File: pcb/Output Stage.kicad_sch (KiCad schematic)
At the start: 18 parts

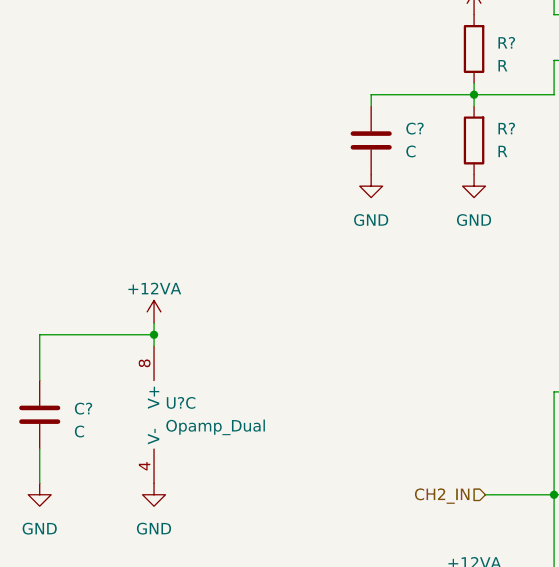
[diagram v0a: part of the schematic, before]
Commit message: Completed schematic oranization and components connection
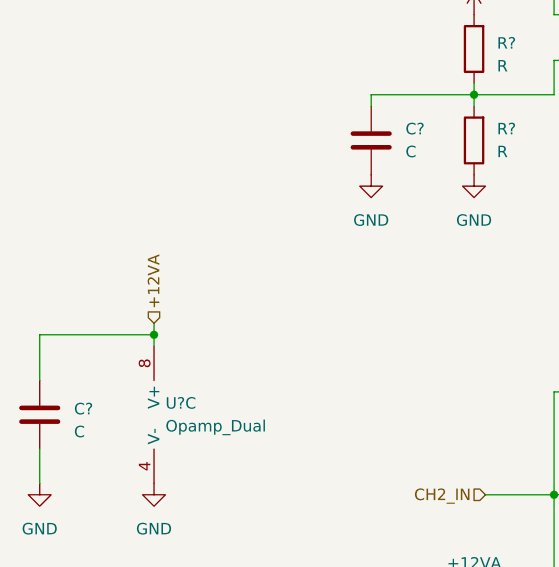
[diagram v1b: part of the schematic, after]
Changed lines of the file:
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@@
+    (effects (font (size 1.27 1.27)) (justify left))
+  )
+  (hierarchical_label "+12VA" (shape input) (at 54.61 97.79 90) (fields_autoplaced)
     (effects (font (size 1.27 1.27)) (justify left))
   )
@@
         )
       )
-    )
-  )
-  (symbol (lib_id "power:+12VA") (at 54.61 97.79 0) (unit 1)
-    (in_bom yes) (on_board yes) (dnp no) (fields_autoplaced)
-    (property "Reference" "#PWR02" (at 54.61 101.6 0)
-      (effects (font (size 1.27 1.27)) hide)
-    )
-    (property "Value" "+12VA" (at 54.61 93.98 0)
-      (effects (font (size 1.27 1.27)))
-    )
-    (property "Footprint" "" (at 54.61 97.79 0)
-      (effects (font (size 1.27 1.27)) hide)
-    )
-    (property "Datasheet" "" (at 54.61 97.79 0)
-      (effects (font (size 1.27 1.27)) hide)
-    )
-    (pin "1")
-    (instances
-      (project "Signal Generator"
-        (path "/f6255c48-6253-4c69-a6db-1ceaf4eff04d"
-          (reference "#PWR02") (unit 1)
-        )
-        (path "/f6255c48-6253-4c69-a6db-1ceaf4eff04d/d7478301-eb73-4c22-aaa0-fe451be16808"
-          (reference "#PWR0117") (unit 1)
-        )
-      )

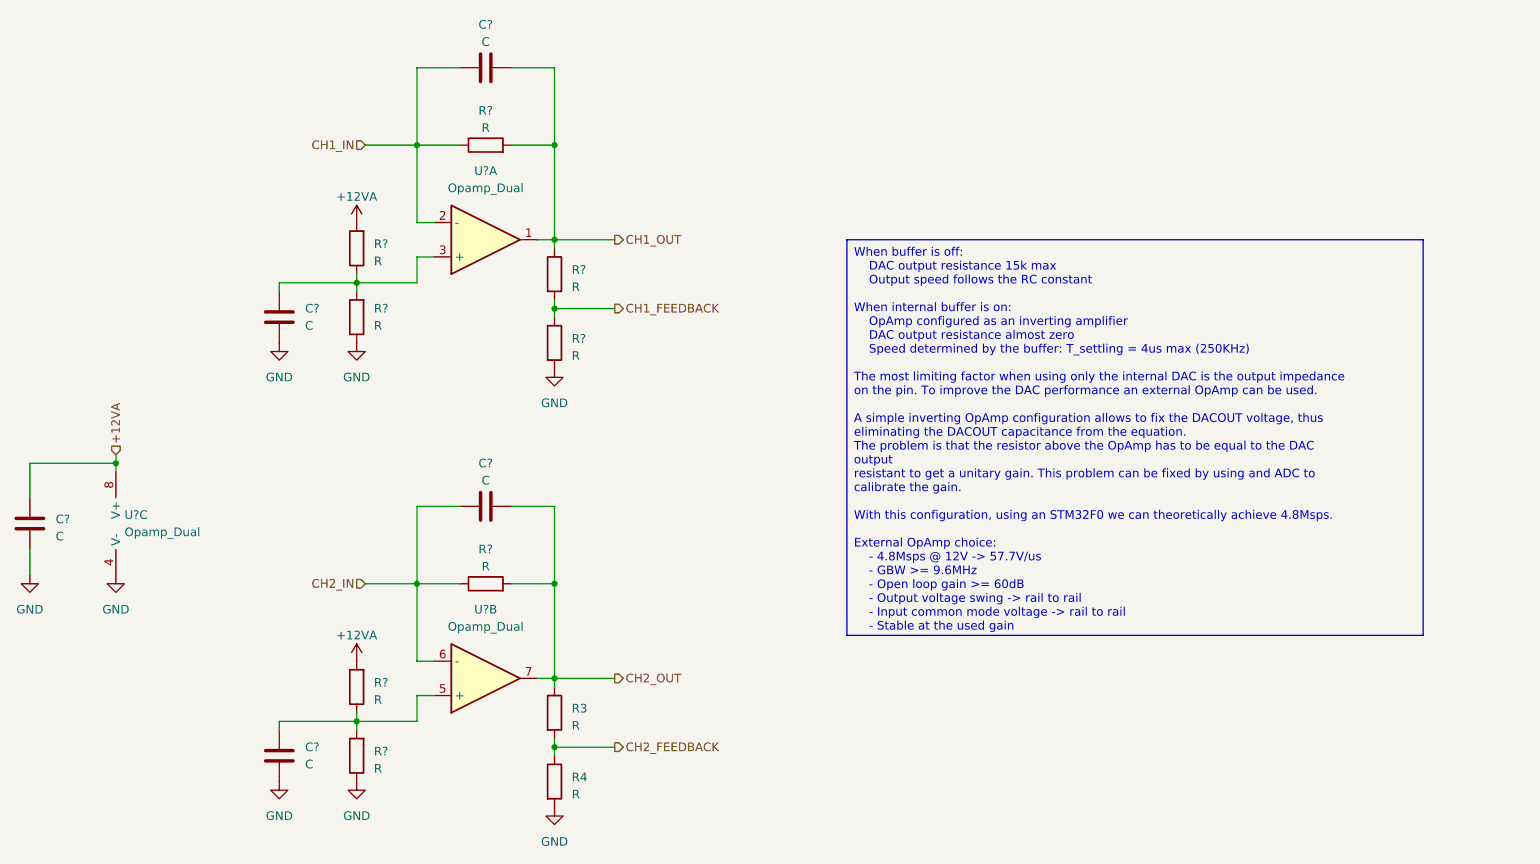
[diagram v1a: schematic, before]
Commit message: Added micro SD and RGB led to schematic. Also added components part numbers
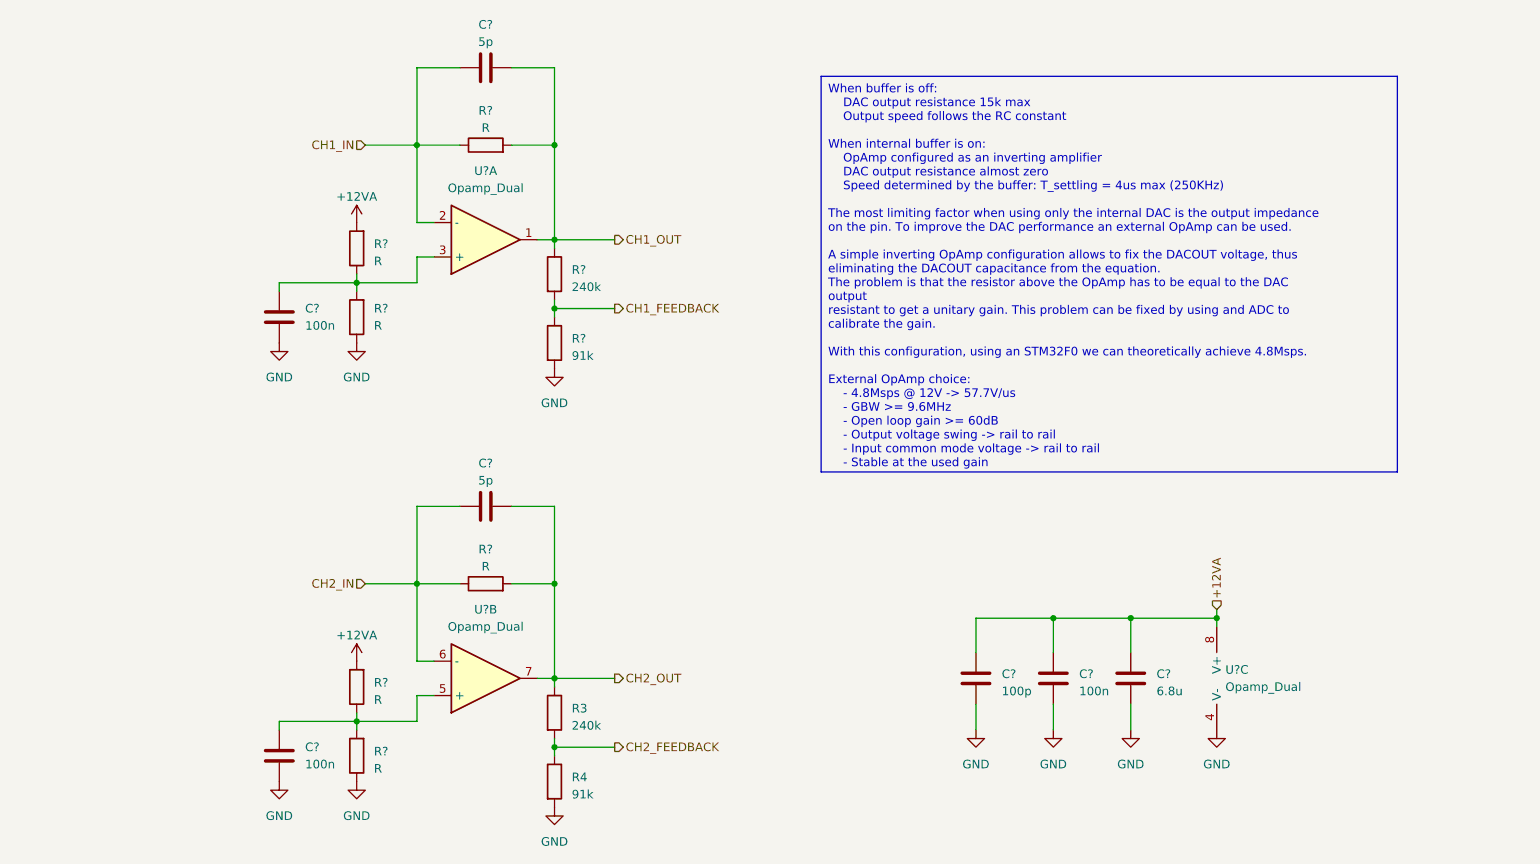
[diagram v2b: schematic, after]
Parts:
- added C?: 100n, Capacitor_SMD:C_0603_1608Metric, symbol Device:C
- added C?: 100p, Capacitor_SMD:C_0603_1608Metric, symbol Device:C
- C? (x2): value C -> 5p; PN (none) -> GQM1875C2E5R0CB12D
- C?: value C -> 6.8u; PN (none) -> GRM1885C1H6R8CA1D
- C? (x2): value C -> 100n; PN (none) -> GCM188R71H104KA57J
- R3, R?: value R -> 240k; PN (none) -> ERJ-3RED2403V
- R4, R?: value R -> 91k; PN (none) -> ERJ-PB3B9102V
- U? (x3): PN (none) -> SN10502D
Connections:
- net +12VA: now also C?.1, C?.1
- net GND: now also C?.2, C?.2
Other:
- moved on the sheet: C?, U?C

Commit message: Completed schematic and tried some simulations
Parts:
- removed C? (x2): 5p, Capacitor_SMD:C_0603_1608Metric, symbol Device:C
- added C? (x2): 0.5p, Capacitor_SMD:C_0603_1608Metric, symbol Device:C
- C?: PN GRM1885C1H6R8CA1D -> GRM1885C1H6R8CA01D
- R? (x2): value R -> 1.33k; PN (none) -> ERJ-PB3B1331V
- R? (x2): value R -> 4.75k; PN (none) -> ERJ-PB3B4751V
- R? (x2): value R -> 46.4k; PN (none) -> ERJ-PB3B4642V
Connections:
- net CH1_IN: now also C?.1
- net CH1_OUT: now also C?.2
- net CH2_IN: now also C?.1
- net CH2_OUT: now also C?.2

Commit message: Completed PCB and prepared production files
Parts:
- U? (x3): PN SN10502D -> OPA2810IDR
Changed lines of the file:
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@@
       (effects (font (size 1.27 1.27)) hide)
     )
-    (property "PN" "SN10502D" (at 109.22 66.04 0)
+    (property "PN" "OPA2810IDR" (at 109.22 66.04 0)
       (effects (font (size 1.27 1.27)) hide)
     )
@@
       (effects (font (size 1.27 1.27)) hide)
     )
-    (property "PN" "SN10502D" (at 109.22 130.81 0)
+    (property "PN" "OPA2810IDR" (at 109.22 130.81 0)
       (effects (font (size 1.27 1.27)) hide)
     )
@@
       (effects (font (size 1.27 1.27)) hide)
     )
-    (property "PN" "SN10502D" (at 219.71 130.81 0)
-      (effects (font (size 1.27 1.27)) hide)
-    )
+    (property "PN" "OPA2810IDR" (at 219.71 130.81 0)
+      (effects (font (size 1.27 1.27)) hide)
+    )

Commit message: Fixed FTDI connection to the stm32
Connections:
- net CH1_FEEDBACK: now also R3.2, R4.1; no longer R?.1, R?.2
- net CH1_IN: now also C?.1, R?.1, U?.6 (-); no longer C?.1, R?.1, U?.2 (-)
- net CH1_OUT: now also C?.2, R3.1, R?.2, U?.7; no longer C?.2, R?.1, R?.2, U?.1
- net CH2_FEEDBACK: now also R?.1, R?.2; no longer R3.2, R4.1
- net CH2_IN: now also C?.1, R?.1, U?.2 (-); no longer C?.1, R?.1, U?.6 (-)
- net CH2_OUT: now also C?.2, R?.1, R?.2, U?.1; no longer C?.2, R3.1, R?.2, U?.7
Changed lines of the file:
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@@
     (effects (font (size 1.27 1.27)) (justify left top))
   )
-  (hierarchical_label "CH1_OUT" (shape output) (at 128.27 66.04 0) (fields_autoplaced)
+  (hierarchical_label "CH2_OUT" (shape output) (at 128.27 66.04 0) (fields_autoplaced)
     (effects (font (size 1.27 1.27)) (justify left))
   )
@@
     (effects (font (size 1.27 1.27)) (justify left))
   )
-  (hierarchical_label "CH2_IN" (shape input) (at 91.44 116.84 180) (fields_autoplaced)
+  (hierarchical_label "CH1_IN" (shape input) (at 91.44 116.84 180) (fields_autoplaced)
     (effects (font (size 1.27 1.27)) (justify right))
   )
-  (hierarchical_label "CH2_OUT" (shape output) (at 128.27 130.81 0) (fields_autoplaced)
+  (hierarchical_label "CH1_OUT" (shape output) (at 128.27 130.81 0) (fields_autoplaced)
     (effects (font (size 1.27 1.27)) (justify left))
   )
-  (hierarchical_label "CH2_FEEDBACK" (shape output) (at 128.27 140.97 0) (fields_autoplaced)
+  (hierarchical_label "CH1_FEEDBACK" (shape output) (at 128.27 140.97 0) (fields_autoplaced)
     (effects (font (size 1.27 1.27)) (justify left))
   )
-  (hierarchical_label "CH1_FEEDBACK" (shape output) (at 128.27 76.2 0) (fields_autoplaced)
+  (hierarchical_label "CH2_FEEDBACK" (shape output) (at 128.27 76.2 0) (fields_autoplaced)
     (effects (font (size 1.27 1.27)) (justify left))
   )
-  (hierarchical_label "CH1_IN" (shape input) (at 91.44 52.07 180) (fields_autoplaced)
+  (hierarchical_label "CH2_IN" (shape input) (at 91.44 52.07 180) (fields_autoplaced)
     (effects (font (size 1.27 1.27)) (justify right))
   )
